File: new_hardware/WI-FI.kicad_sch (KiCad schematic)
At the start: 15 parts

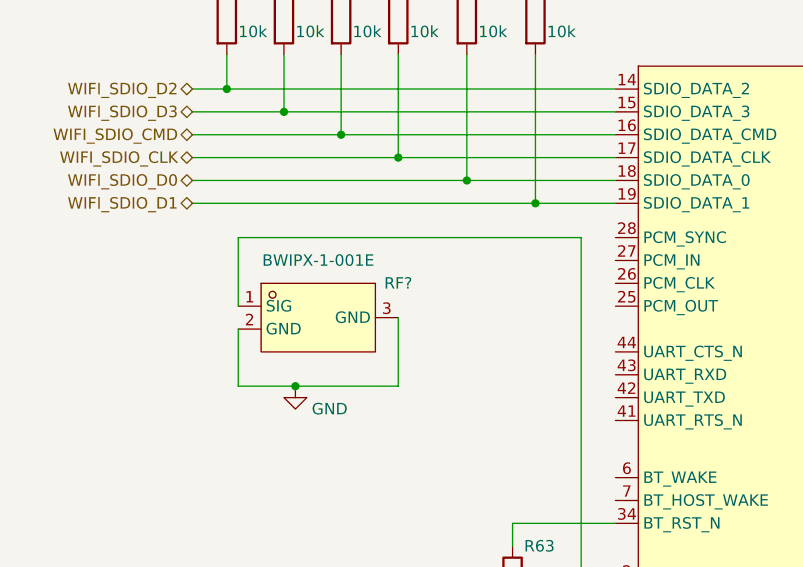
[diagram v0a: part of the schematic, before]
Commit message: removed some unused files
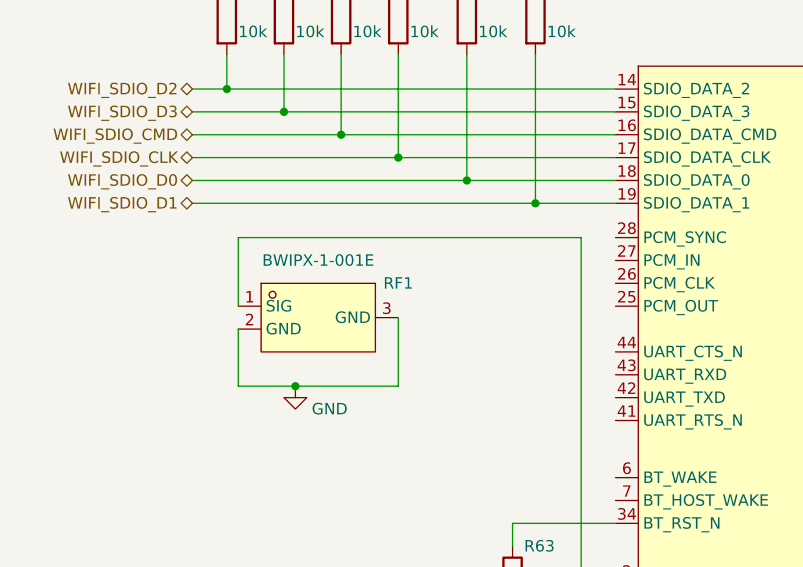
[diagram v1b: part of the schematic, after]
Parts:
- gave numbers to parts that had none: 1
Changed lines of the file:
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@@
   (symbol (lib_id "rlib_connectors:BWIPX-1-001E") (at 88.9 74.93 0) (unit 1)
     (in_bom yes) (on_board yes)
-    (property "Reference" "RF?" (id 0) (at 97.79 71.12 0))
+    (property "Reference" "RF1" (id 0) (at 97.79 71.12 0))
     (property "Value" "BWIPX-1-001E" (id 1) (at 88.9 68.58 0))
     (property "Footprint" "rlib_connectors:IPEX-SMD_BWIPX-1-001E" (id 2) (at 88.9 83.82 0)
@@
   (symbol (lib_id "power:GND") (at 86.36 82.55 0) (unit 1)
     (in_bom yes) (on_board yes)
-    (property "Reference" "#PWR?" (id 0) (at 86.36 88.9 0)
+    (property "Reference" "#PWR0143" (id 0) (at 86.36 88.9 0)
       (effects (font (size 1.27 1.27)) hide)
     )

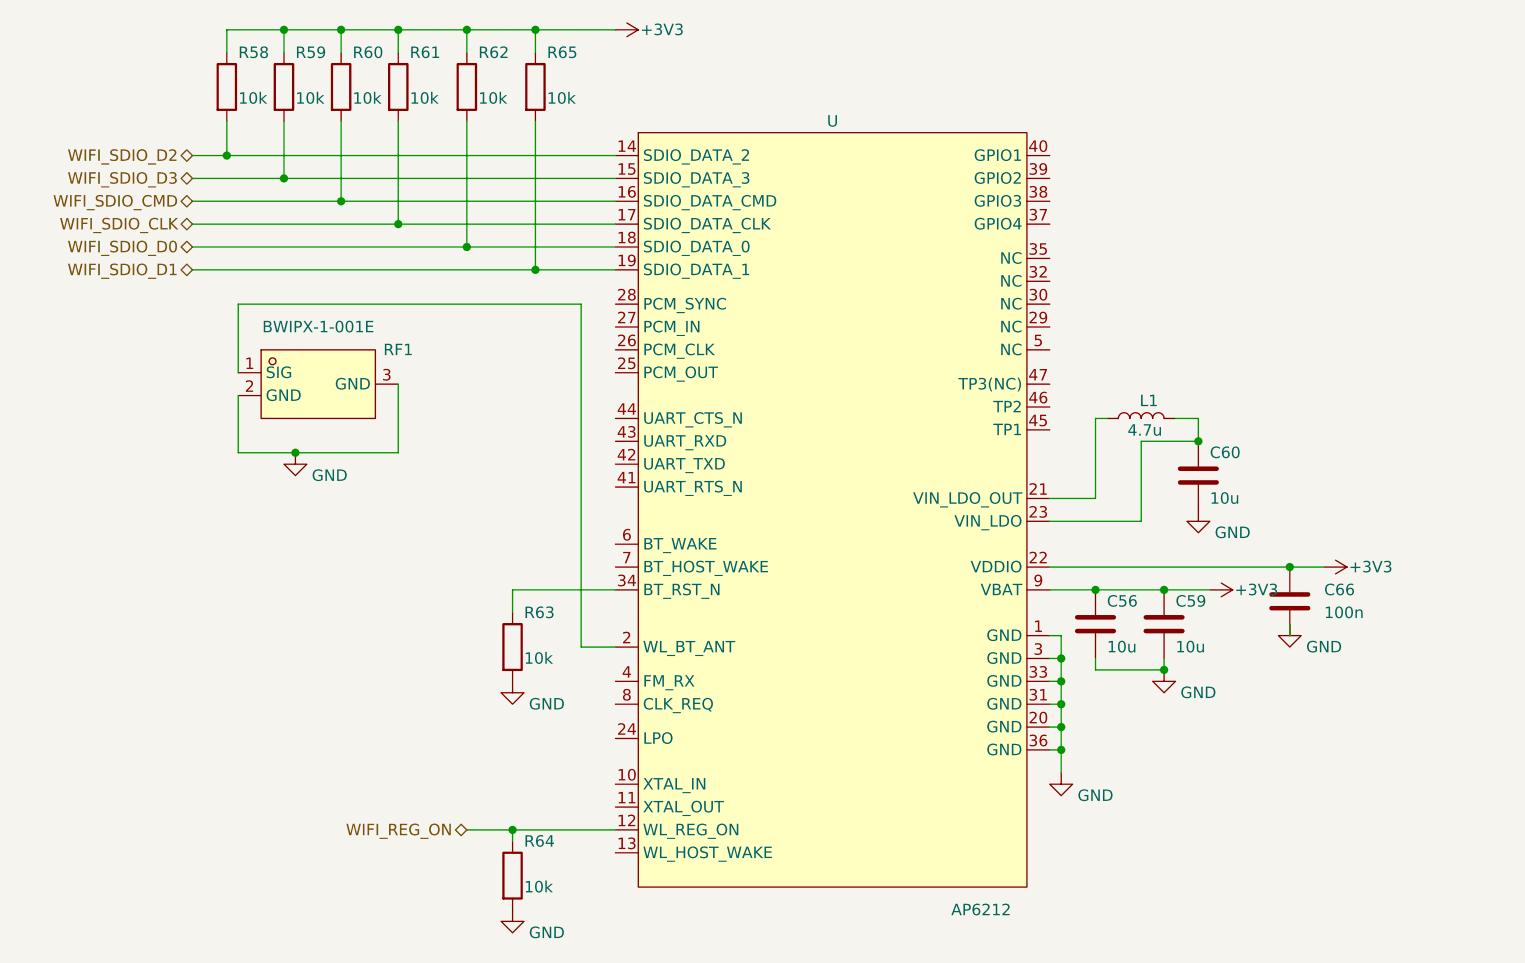
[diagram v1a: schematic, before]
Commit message: wi-fi module is moved to closer board outline,unused files are removed
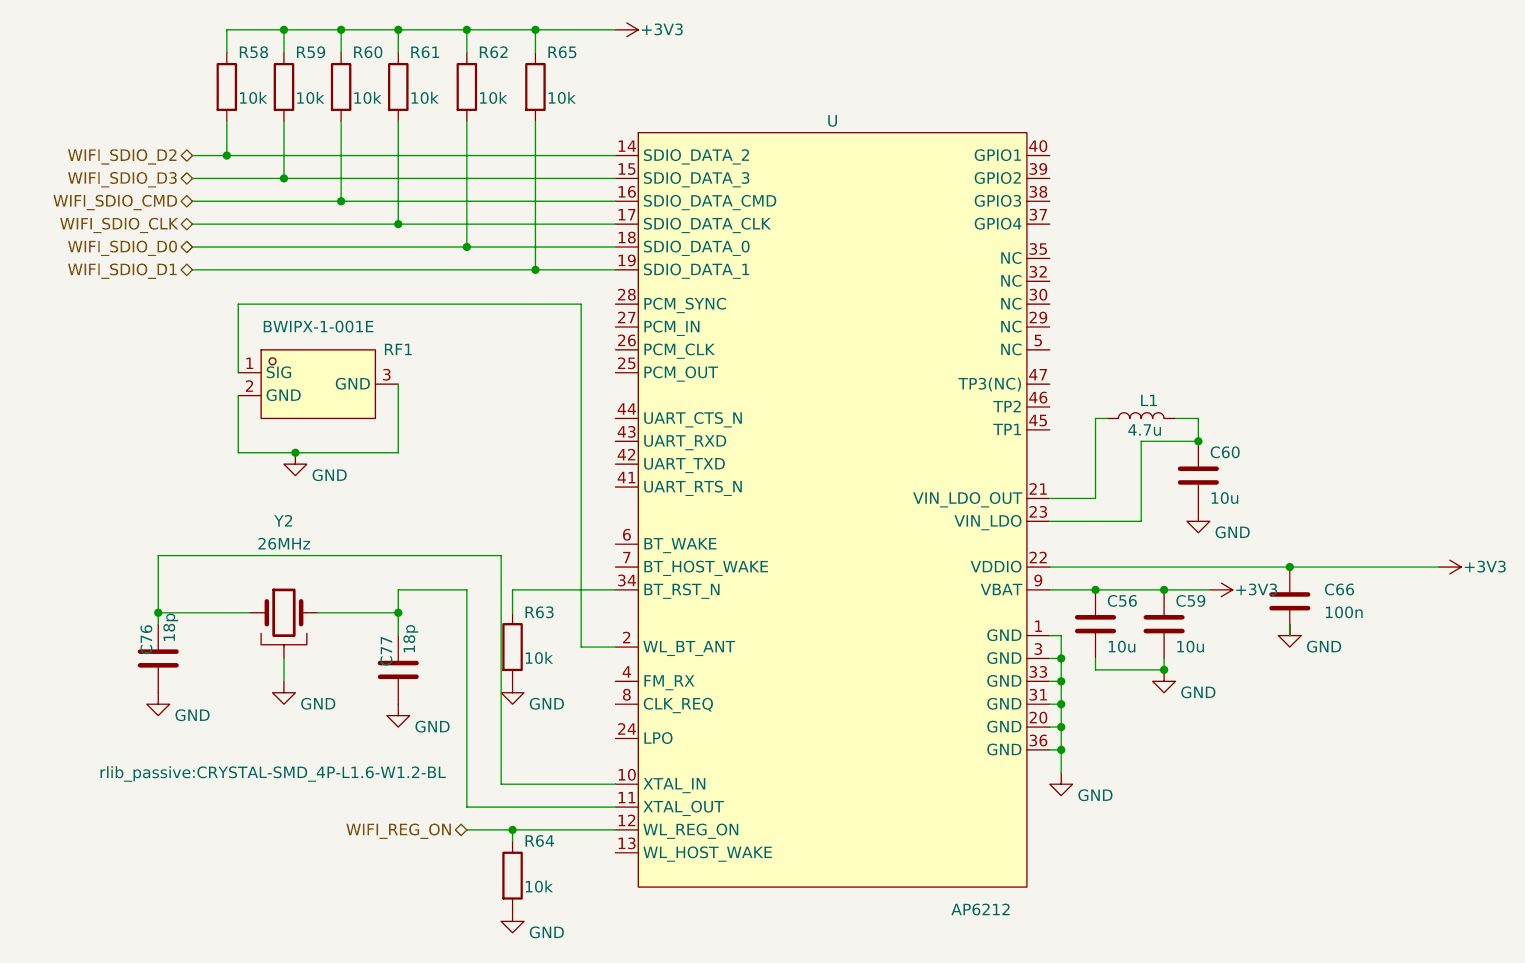
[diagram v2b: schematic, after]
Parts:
- added C76, C77: 18p, rlib_passive:C_0603_1608Metric, symbol rlib_passive:C
- added Y2: 26МHz, rlib_passive:CRYSTAL-SMD_4P-L1.6-W1.2-BL, symbol rlib_passive:26МHz
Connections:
- net GND: now also C76.1, C77.1, Y2.3
- net at U.10 (XTAL_IN): now also C76.2, Y2.1
- net at U.11 (XTAL_OUT): now also C77.2, Y2.2
